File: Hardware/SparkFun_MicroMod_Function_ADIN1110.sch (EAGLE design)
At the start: 81 parts, among them J1 T1_INDUSTRIAL, J2 MICROMOD_FUNCTION_STANDARD, Q1 220mA/50V/3.5Ω, Q2 20V/4.2A/52mΩ/1.4W, T1 WE-STST, U1 ADIN1110, U2 EEPROM, U3 3.3V, U4 WE-TVS, Y1 25MHz

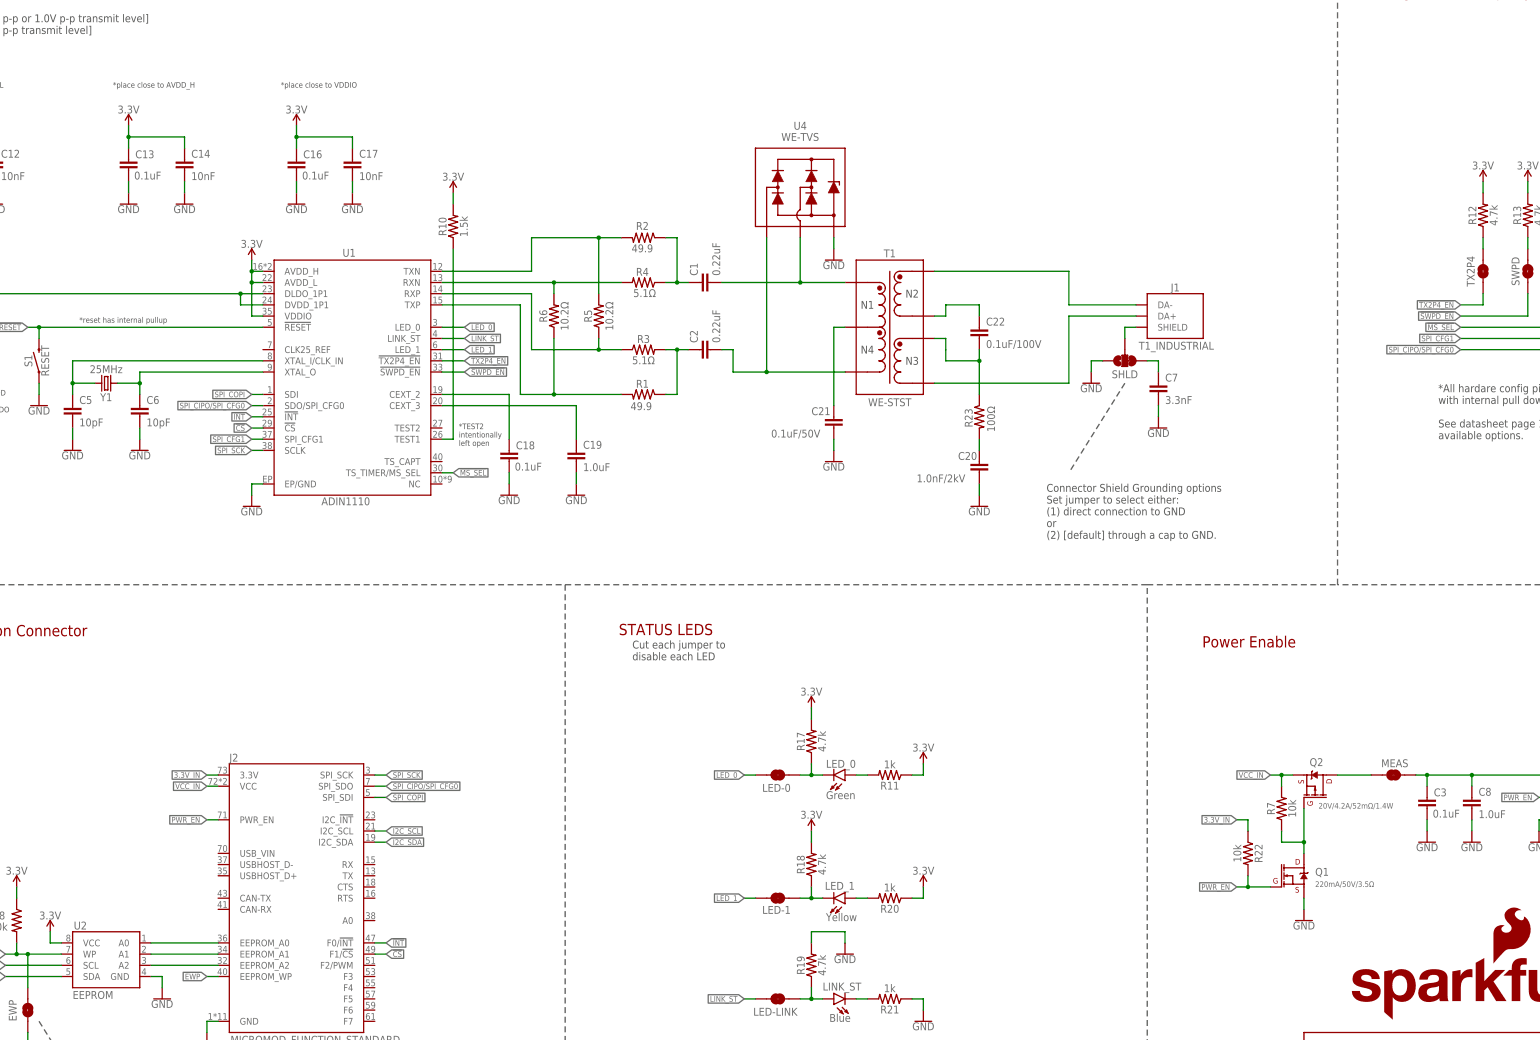
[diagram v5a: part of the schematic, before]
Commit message: checklist catches
-added CS and INT pulllups
-nudged vias to avoid silk
-added 1/2/3/4 text objects to help indicate 4 layers
-added suggested Selective Solder path on layer 48
-adjusted tnames for better assembly sheet
-added measures
-corrected active low labels on some bottom config jumpers
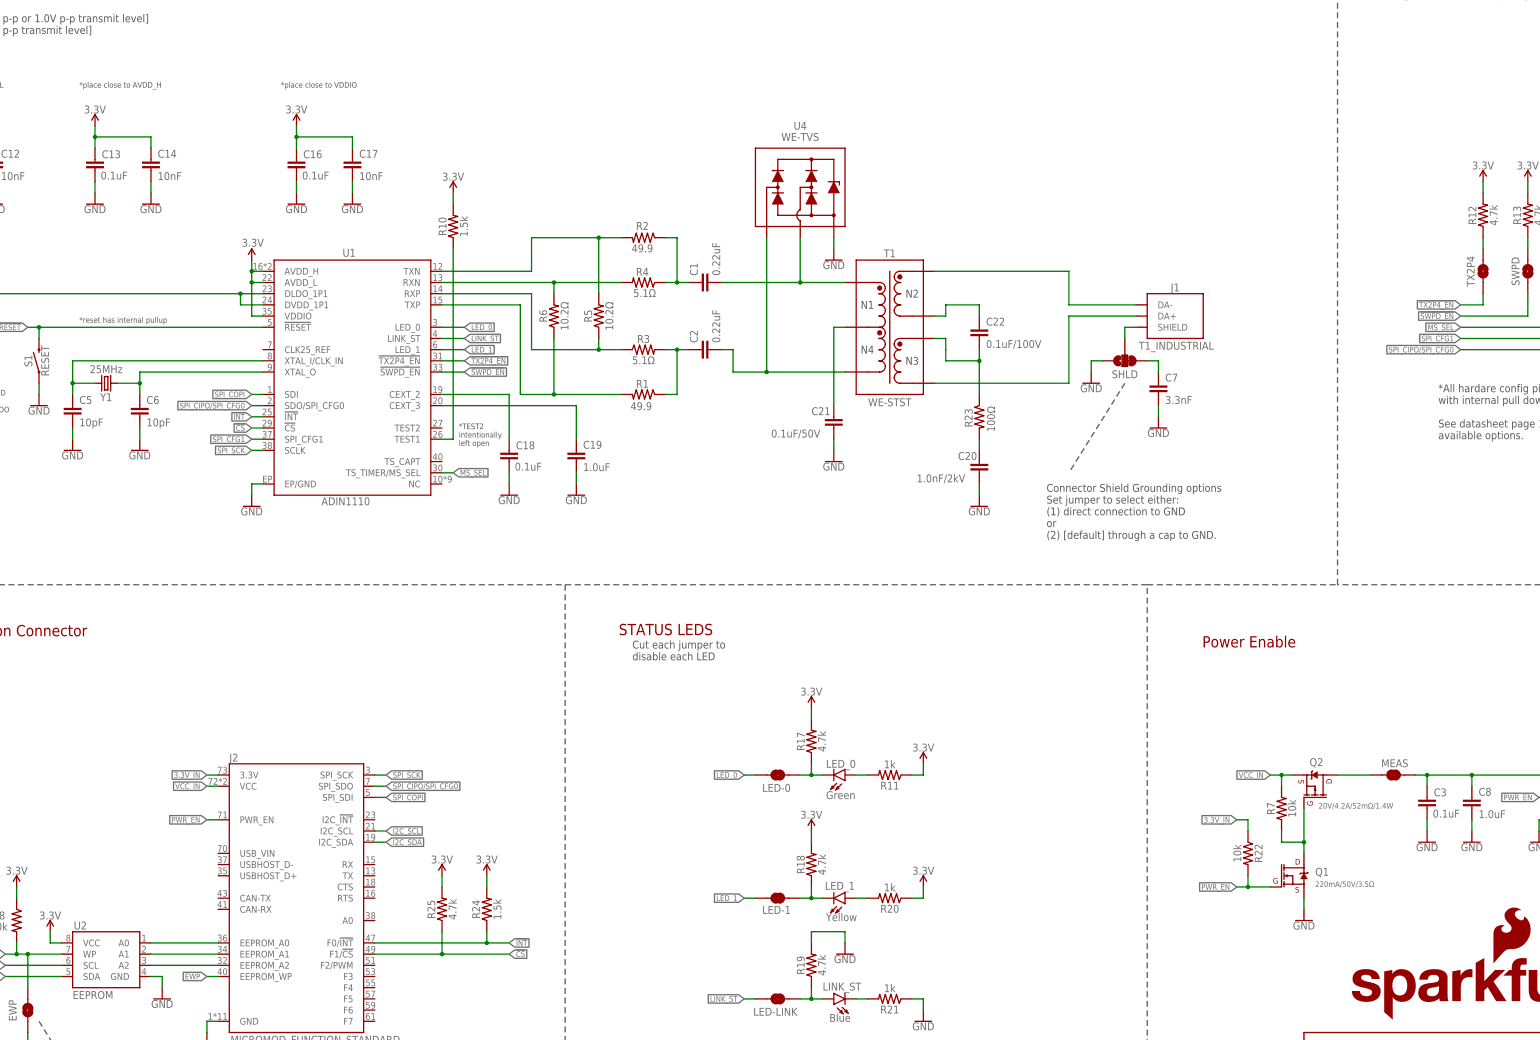
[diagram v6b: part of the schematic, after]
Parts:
- added R24: 1.5k, SparkFun-Resistors:1.5KOHM-0603-1/10W-1%
- added R25: 4.7k, SparkFun-Resistors:4.7KOHM-0402T-1/16W-1%
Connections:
- net !MS_SEL! renamed MS_SEL
- net !CS!: now also R25.1
- net !INT!: now also R24.1
- net 3.3V: now also R24.2, R25.2
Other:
- moved on the sheet: C13, C14
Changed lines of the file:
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@@
 <part name="LED-1" library="SparkFun-Jumpers" deviceset="JUMPER-SMT_2_NC_TRACE" device="_SILK" package3d_urn="urn:adsk.eagle:package:39281/1" value="JUMPER-SMT_2_NC_TRACE_SILK"/>
 <part name="LED-0" library="SparkFun-Jumpers" deviceset="JUMPER-SMT_2_NC_TRACE" device="_SILK" package3d_urn="urn:adsk.eagle:package:39281/1" value="JUMPER-SMT_2_NC_TRACE_SILK"/>
+<part name="R24" library="SparkFun-Resistors" deviceset="1.5KOHM" device="-0603-1/10W-1%" value="1.5k"/>
+<part name="SUPPLY2" library="SparkFun-PowerSymbols" deviceset="3.3V" device=""/>
+<part name="R25" library="SparkFun-Resistors" deviceset="4.7KOHM" device="-0402T-1/16W-1%" value="4.7k"/>
+<part name="SUPPLY3" library="SparkFun-PowerSymbols" deviceset="3.3V" device=""/>
 </parts>
 <sheets>
@@
 *place C11 (0.68uF) close to DLDO</text>
 <text x="16.764" y="249.936" size="1.27" layer="97" font="vector">*place close to AVDD_L</text>
-<text x="59.944" y="249.936" size="1.27" layer="97" font="vector">*place close to AVDD_H</text>
+<text x="52.324" y="249.936" size="1.27" layer="97" font="vector">*place close to AVDD_H</text>
 <text x="98.044" y="249.936" size="1.27" layer="97" font="vector">*place close to VDDIO</text>
 <text x="138.43" y="173.736" size="1.27" layer="97" font="vector" align="top-left">*TEST2
@@
 </instance>
 <instance part="SUPPLY18" gate="G$1" x="91.44" y="210.82" smashed="yes">
-<attribute name="VALUE" x="91.44" y="213.614" size="1.778" layer="96" font="vector" align="bottom-center"/>
+<attribute name="VALUE" x="91.694" y="213.868" size="1.778" layer="96" font="vector" align="bottom-center"/>
 </instance>
 <instance part="GND34" gate="1" x="91.44" y="154.94" smashed="yes">
@@
 <attribute name="VALUE" x="20.32" y="244.094" size="1.778" layer="96" font="vector" align="bottom-center"/>
 </instance>
-<instance part="C13" gate="G$1" x="63.5" y="231.14" smashed="yes" rot="MR0">
-<attribute name="NAME" x="65.024" y="233.934" size="1.778" layer="95" font="vector"/>
-<attribute name="VALUE" x="64.77" y="229.108" size="1.778" layer="96" font="vector"/>
-</instance>
-<instance part="GND39" gate="1" x="63.5" y="223.52" smashed="yes">
-<attribute name="VALUE" x="63.5" y="223.266" size="1.778" layer="96" font="vector" align="top-center"/>
-</instance>
-<instance part="C14" gate="G$1" x="76.2" y="231.14" smashed="yes">
-<attribute name="NAME" x="77.724" y="234.061" size="1.778" layer="95" font="vector"/>
-<attribute name="VALUE" x="77.724" y="228.981" size="1.778" layer="96" font="vector"/>
-</instance>
-<instance part="GND40" gate="1" x="76.2" y="223.52" smashed="yes">
-<attribute name="VALUE" x="76.2" y="223.266" size="1.778" layer="96" font="vector" align="top-center"/>
-</instance>
-<instance part="SUPPLY20" gate="G$1" x="63.5" y="241.3" smashed="yes">
-<attribute name="VALUE" x="63.5" y="244.094" size="1.778" layer="96" font="vector" align="bottom-center"/>
+<instance part="C13" gate="G$1" x="55.88" y="231.14" smashed="yes" rot="MR0">
+<attribute name="NAME" x="57.404" y="233.934" size="1.778" layer="95" font="vector"/>
+<attribute name="VALUE" x="57.15" y="229.108" size="1.778" layer="96" font="vector"/>
+</instance>
+<instance part="GND39" gate="1" x="55.88" y="223.52" smashed="yes">
+<attribute name="VALUE" x="55.88" y="223.266" size="1.778" layer="96" font="vector" align="top-center"/>
+</instance>
+<instance part="C14" gate="G$1" x="68.58" y="231.14" smashed="yes">
+<attribute name="NAME" x="70.104" y="234.061" size="1.778" layer="95" font="vector"/>
+<attribute name="VALUE" x="70.104" y="228.981" size="1.778" layer="96" font="vector"/>
+</instance>
+<instance part="GND40" gate="1" x="68.58" y="223.52" smashed="yes">
+<attribute name="VALUE" x="68.58" y="223.266" size="1.778" layer="96" font="vector" align="top-center"/>
+</instance>
+<instance part="SUPPLY20" gate="G$1" x="55.88" y="241.3" smashed="yes">
+<attribute name="VALUE" x="55.88" y="244.094" size="1.778" layer="96" font="vector" align="bottom-center"/>
 </instance>
 <instance part="C15" gate="G$1" x="12.7" y="195.58" smashed="yes" rot="MR0">
@@
 <instance part="LED-0" gate="G$1" x="210.82" y="93.98" smashed="yes" rot="R180">
 <attribute name="NAME" x="207.264" y="90.17" size="1.778" layer="95" font="vector"/>
+</instance>
+<instance part="R24" gate="G$1" x="144.78" y="63.5" smashed="yes" rot="R90">
+<attribute name="NAME" x="143.256" y="63.5" size="1.778" layer="95" font="vector" rot="R90" align="bottom-center"/>
+<attribute name="VALUE" x="146.304" y="63.5" size="1.778" layer="96" font="vector" rot="R90" align="top-center"/>
+</instance>
+<instance part="SUPPLY2" gate="G$1" x="144.78" y="71.12" smashed="yes">
+<attribute name="VALUE" x="144.78" y="73.914" size="1.778" layer="96" font="vector" align="bottom-center"/>
+</instance>
+<instance part="R25" gate="G$1" x="134.62" y="63.5" smashed="yes" rot="R90">
+<attribute name="NAME" x="133.096" y="63.5" size="1.778" layer="95" font="vector" rot="R90" align="bottom-center"/>
+<attribute name="VALUE" x="136.144" y="63.5" size="1.778" layer="96" font="vector" rot="R90" align="top-center"/>
+</instance>
+<instance part="SUPPLY3" gate="G$1" x="134.62" y="71.12" smashed="yes">
+<attribute name="VALUE" x="134.62" y="73.914" size="1.778" layer="96" font="vector" align="bottom-center"/>
 </instance>
 </instances>
@@
 <pinref part="C13" gate="G$1" pin="2"/>
 <pinref part="GND39" gate="1" pin="GND"/>
-<wire x1="63.5" y1="226.06" x2="63.5" y2="228.6" width="0.1524" layer="91"/>
+<wire x1="55.88" y1="226.06" x2="55.88" y2="228.6" width="0.1524" layer="91"/>
 </segment>
 <segment>
 <pinref part="GND40" gate="1" pin="GND"/>
 <pinref part="C14" gate="G$1" pin="2"/>
-<wire x1="76.2" y1="226.06" x2="76.2" y2="228.6" width="0.1524" layer="91"/>
+<wire x1="68.58" y1="226.06" x2="68.58" y2="228.6" width="0.1524" layer="91"/>
 </segment>
 <segment>
@@
 <pinref part="SUPPLY20" gate="G$1" pin="3.3V"/>
 <pinref part="C13" gate="G$1" pin="1"/>
-<wire x1="63.5" y1="236.22" x2="63.5" y2="238.76" width="0.1524" layer="91"/>
+<wire x1="55.88" y1="236.22" x2="55.88" y2="238.76" width="0.1524" layer="91"/>
 <pinref part="C14" gate="G$1" pin="1"/>
-<wire x1="63.5" y1="238.76" x2="63.5" y2="241.3" width="0.1524" layer="91"/>
-<wire x1="76.2" y1="236.22" x2="76.2" y2="238.76" width="0.1524" layer="91"/>
-<wire x1="76.2" y1="238.76" x2="63.5" y2="238.76" width="0.1524" layer="91"/>
-<junction x="63.5" y="238.76"/>
+<wire x1="55.88" y1="238.76" x2="55.88" y2="241.3" width="0.1524" layer="91"/>
+<wire x1="68.58" y1="236.22" x2="68.58" y2="238.76" width="0.1524" layer="91"/>
+<wire x1="68.58" y1="238.76" x2="55.88" y2="238.76" width="0.1524" layer="91"/>
+<junction x="55.88" y="238.76"/>
 </segment>
 <segment>
@@
 <pinref part="R20" gate="G$1" pin="1"/>
 <wire x1="243.84" y1="66.04" x2="241.3" y2="66.04" width="0.1524" layer="91"/>
+</segment>
+<segment>
+<pinref part="SUPPLY2" gate="G$1" pin="3.3V"/>
+<wire x1="144.78" y1="71.12" x2="144.78" y2="68.58" width="0.1524" layer="91"/>
+<pinref part="R24" gate="G$1" pin="2"/>
+</segment>
+<segment>
+<pinref part="SUPPLY3" gate="G$1" pin="3.3V"/>
+<wire x1="134.62" y1="68.58" x2="134.62" y2="71.12" width="0.1524" layer="91"/>
+<pinref part="R25" gate="G$1" pin="2"/>
 </segment>
 </net>
@@
 <segment>
 <pinref part="U1" gate="U1" pin="!INT!"/>
+<label x="91.44" y="175.26" size="1.27" layer="95" font="vector" rot="R180" xref="yes"/>
 <wire x1="93.98" y1="175.26" x2="91.44" y2="175.26" width="0.1524" layer="91"/>
-<label x="91.44" y="175.26" size="1.27" layer="95" font="vector" rot="R180" xref="yes"/>
-</segment>
-<segment>
-<label x="121.92" y="55.88" size="1.27" layer="95" font="vector" xref="yes"/>
+</segment>
+<segment>
+<label x="149.86" y="55.88" size="1.27" layer="95" font="vector" xref="yes"/>
 <pinref part="J2" gate="J1" pin="F0/!INT!"/>
-<wire x1="121.92" y1="55.88" x2="119.38" y2="55.88" width="0.1524" layer="91"/>
+<wire x1="149.86" y1="55.88" x2="144.78" y2="55.88" width="0.1524" layer="91"/>
+<pinref part="R24" gate="G$1" pin="1"/>
+<wire x1="144.78" y1="55.88" x2="119.38" y2="55.88" width="0.1524" layer="91"/>
+<wire x1="144.78" y1="55.88" x2="144.78" y2="58.42" width="0.1524" layer="91"/>
+<junction x="144.78" y="55.88"/>
 </segment>
 </net>
@@
 </segment>
 <segment>
-<label x="121.92" y="53.34" size="1.27" layer="95" font="vector" xref="yes"/>
+<label x="149.86" y="53.34" size="1.27" layer="95" font="vector" xref="yes"/>
 <pinref part="J2" gate="J1" pin="F1/!CS!"/>
-<wire x1="121.92" y1="53.34" x2="119.38" y2="53.34" width="0.1524" layer="91"/>
+<wire x1="149.86" y1="53.34" x2="134.62" y2="53.34" width="0.1524" layer="91"/>
+<pinref part="R25" gate="G$1" pin="1"/>
+<wire x1="134.62" y1="53.34" x2="119.38" y2="53.34" width="0.1524" layer="91"/>
+<wire x1="134.62" y1="53.34" x2="134.62" y2="58.42" width="0.1524" layer="91"/>
+<junction x="134.62" y="53.34"/>
 </segment>
 </net>
@@
 </segment>
 </net>
-<net name="!MS_SEL!" class="0">
+<net name="MS_SEL" class="0">
 <segment>
 <pinref part="U1" gate="U1" pin="TS_TIMER/MS_SEL"/>

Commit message: connected RESET to MM GPIO (F5)
-needed for testing, but also could be useful for the user to perform a hard reset on the ANIN1110 from GPIO controlled on their MM main board.
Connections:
- net !RESET!: now also J2.F5
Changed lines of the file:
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@@
 <junction x="43.18" y="195.58"/>
+</segment>
+<segment>
+<pinref part="J2" gate="J1" pin="F5"/>
+<wire x1="119.38" y1="43.18" x2="121.92" y2="43.18" width="0.1524" layer="91"/>
+<label x="121.92" y="43.18" size="1.27" layer="95" xref="yes"/>
 </segment>
 </net>
